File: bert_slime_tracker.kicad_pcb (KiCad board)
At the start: 2 copper layers, 35 x 42.5 mm, 25 parts, among them CN1 SM05B-SRSS-TB (LF)(SN), SW1 MK-12C02-G020, U1 ICM-45686, U2 QMC6309, Y1 1532H-24.000JWVDTL

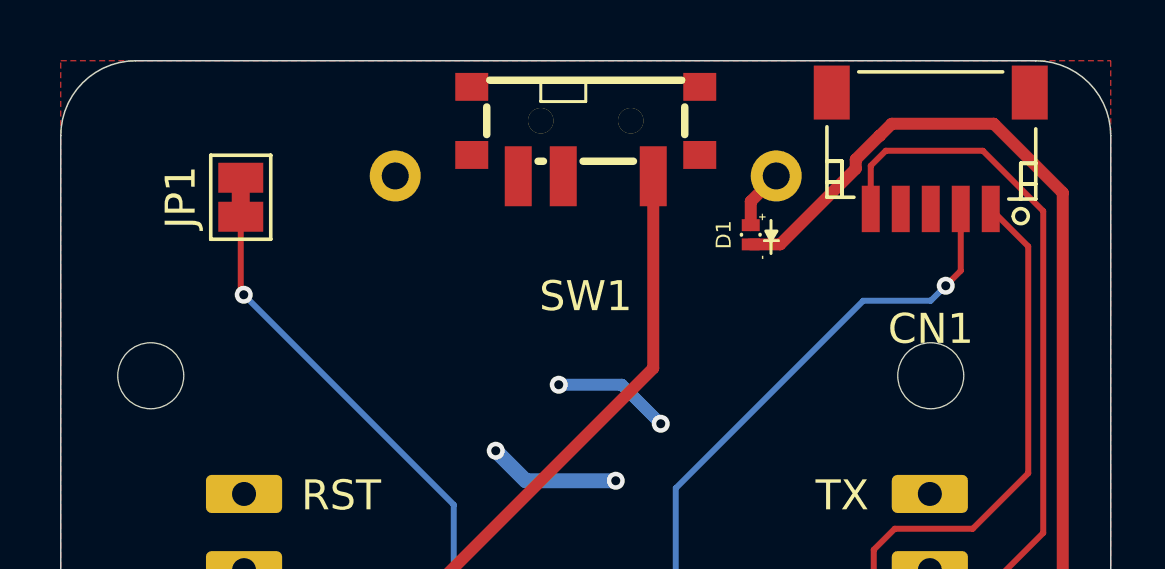
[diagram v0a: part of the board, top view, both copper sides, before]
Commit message: updated to corrected oscillator
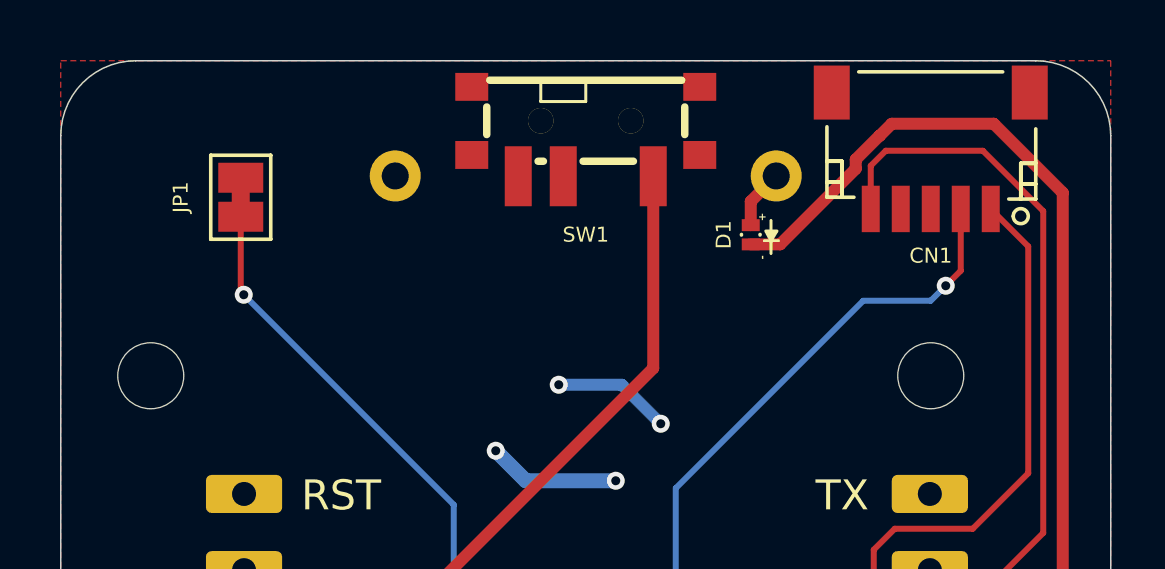
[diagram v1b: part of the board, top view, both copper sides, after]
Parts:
- Y1: value 1532H-24.000JWVDTL -> 32.768 kHz Oscillator
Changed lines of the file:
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@@
 			(effects
 				(font
-					(size 1 1)
-					(thickness 0.15)
+					(size 0.5 0.5)
+					(thickness 0.125)
 				)
 			)
@@
 		(property ki_fp_filters "SolderJumper*Bridged*")
 		(sheetname "/")
-		(sheetfile "slime_tracker.kicad_sch")
+		(sheetfile "bert_slime_tracker.kicad_sch")
 		(zone_connect 1)
 		(attr exclude_from_pos_files exclude_from_bom allow_soldermask_bridges)
@@
 		)
 		(sheetname "/")
-		(sheetfile "slime_tracker.kicad_sch")
+		(sheetfile "bert_slime_tracker.kicad_sch")
 		(attr smd)
 		(fp_line
@@
 		)
 		(sheetname "/")
-		(sheetfile "slime_tracker.kicad_sch")
+		(sheetfile "bert_slime_tracker.kicad_sch")
 		(attr smd)
 		(fp_line
@@
 		)
 		(sheetname "/")
-		(sheetfile "slime_tracker.kicad_sch")
+		(sheetfile "bert_slime_tracker.kicad_sch")
 		(attr smd)
 		(fp_line
@@
 		(property ki_fp_filters "R_*")
 		(sheetname "/")
-		(sheetfile "slime_tracker.kicad_sch")
+		(sheetfile "bert_slime_tracker.kicad_sch")
 		(attr smd)
 		(fp_line
@@
 		(property ki_fp_filters "C_*")
 		(sheetname "/")
-		(sheetfile "slime_tracker.kicad_sch")
+		(sheetfile "bert_slime_tracker.kicad_sch")
 		(attr smd)
 		(fp_line
@@
 		(property ki_fp_filters "R_*")
 		(sheetname "/")
-		(sheetfile "slime_tracker.kicad_sch")
+		(sheetfile "bert_slime_tracker.kicad_sch")
 		(attr smd)
 		(fp_line
@@
 		(at 151.5 73 180)
 		(property "Reference" "CN1"
-			(at 0 -5.94 180)
+			(at 0 -3.5 180)
 			(layer "F.SilkS")
 			(effects
 				(font
-					(size 1 1)
-					(thickness 0.15)
+					(size 0.5 0.5)
+					(thickness 0.125)
 				)
 			)
@@
 		)
 		(sheetname "/")
-		(sheetfile "slime_tracker.kicad_sch")
+		(sheetfile "bert_slime_tracker.kicad_sch")
 		(attr smd)
 		(fp_line
@@
 		(property ki_fp_filters "MountingHole*Pad*")
 		(sheetname "/")
-		(sheetfile "slime_tracker.kicad_sch")
+		(sheetfile "bert_slime_tracker.kicad_sch")
 		(attr exclude_from_pos_files exclude_from_bom)
 		(fp_line
@@
 		)
 		(sheetname "/")
-		(sheetfile "slime_tracker.kicad_sch")
+		(sheetfile "bert_slime_tracker.kicad_sch")
 		(attr through_hole)
 		(fp_rect
@@
 		)
 		(sheetname "/")
-		(sheetfile "slime_tracker.kicad_sch")
+		(sheetfile "bert_slime_tracker.kicad_sch")
 		(attr smd)
 		(fp_poly
@@
 		(property ki_fp_filters "C_*")
 		(sheetname "/")
-		(sheetfile "slime_tracker.kicad_sch")
+		(sheetfile "bert_slime_tracker.kicad_sch")
 		(attr smd)
 		(fp_line
@@
 		(property ki_fp_filters "R_*")
 		(sheetname "/")
-		(sheetfile "slime_tracker.kicad_sch")
+		(sheetfile "bert_slime_tracker.kicad_sch")
 		(attr smd)
 		(fp_line
@@
 		)
 		(sheetname "/")
-		(sheetfile "slime_tracker.kicad_sch")
+		(sheetfile "bert_slime_tracker.kicad_sch")
 		(attr through_hole)
 		(fp_rect
@@
 		(at 140 72.36 180)
 		(property "Reference" "SW1"
-			(at 0 -5.49 180)
+			(at 0 -3.44 180)
 			(layer "F.SilkS")
 			(effects
 				(font
-					(size 1 1)
-					(thickness 0.15)
+					(size 0.5 0.5)
+					(thickness 0.125)
 				)
 			)
@@
 		)
 		(sheetname "/")
-		(sheetfile "slime_tracker.kicad_sch")
+		(sheetfile "bert_slime_tracker.kicad_sch")
 		(attr smd)
 		(fp_line
@@
 		(property ki_fp_filters "MountingHole*Pad*")
 		(sheetname "/")
-		(sheetfile "slime_tracker.kicad_sch")
+		(sheetfile "bert_slime_tracker.kicad_sch")
 		(attr exclude_from_pos_files exclude_from_bom)
 		(fp_line
@@
 		(property ki_fp_filters "R_*")
 		(sheetname "/")
-		(sheetfile "slime_tracker.kicad_sch")
+		(sheetfile "bert_slime_tracker.kicad_sch")
 		(attr smd)
 		(fp_line
@@
 		(property ki_fp_filters "C_*")
 		(sheetname "/")
-		(sheetfile "slime_tracker.kicad_sch")
+		(sheetfile "bert_slime_tracker.kicad_sch")
 		(attr smd)
 		(fp_line
@@
 			)
 		)
-		(property "Value" "1532H-24.000JWVDTL"
+		(property "Value" "32.768 kHz Oscillator"
 			(at 0 2.45 0)
 			(layer "F.Fab")
@@
 			)
 		)
-		(property "Datasheet" "https://jlcpcb.com/api/file/downloadByFileSystemAccessId/8590892673421160448"
+		(property "Datasheet" "https://jlcpcb.com/api/file/downloadByFileSystemAccessId/8590171186467942400"
 			(at 0 0 0)
 			(layer "F.Fab")
@@
 			)
 		)
-		(property "Description" "3.3V ±10ppm ±30ppm HCMOS 8MHz SMD3225-4P Crystal Oscillators"
+		(property "Description" "3.3V 5mA ±20ppm CMOS 32.768kHz SMD3225-4P Crystal Oscillators ROHS"
 			(at 0 0 0)
 			(layer "F.Fab")
@@
 			)
 		)
-		(property "LCSC Part" "C19674145"
+		(property "LCSC Part" "C555607"
 			(at 0 0 180)
 			(unlocked yes)
@@
 		(property ki_fp_filters "Oscillator*SMD*Abracon*ASE*3.2x2.5mm*")
 		(sheetname "/")
-		(sheetfile "slime_tracker.kicad_sch")
+		(sheetfile "bert_slime_tracker.kicad_sch")
 		(attr smd)
 		(fp_line
@@
 		(property ki_fp_filters "R_*")
 		(sheetname "/")
-		(sheetfile "slime_tracker.kicad_sch")
+		(sheetfile "bert_slime_tracker.kicad_sch")
 		(attr smd)
 		(fp_line
